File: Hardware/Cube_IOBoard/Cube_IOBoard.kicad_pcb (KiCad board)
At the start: 2 copper layers, 50.5 x 50.4 mm, 14 parts, among them J10 Pixhawk_Cube_DF17_Module_Bus_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, J11 GPS1 & I2C1, J12 GPS2 & I2C2, J13 TELEM2, J2 USB, LED & BUZZER, J4 ADC, J5 CAN2, J6 I2C2, J7 TELEM1, J8 CAN1

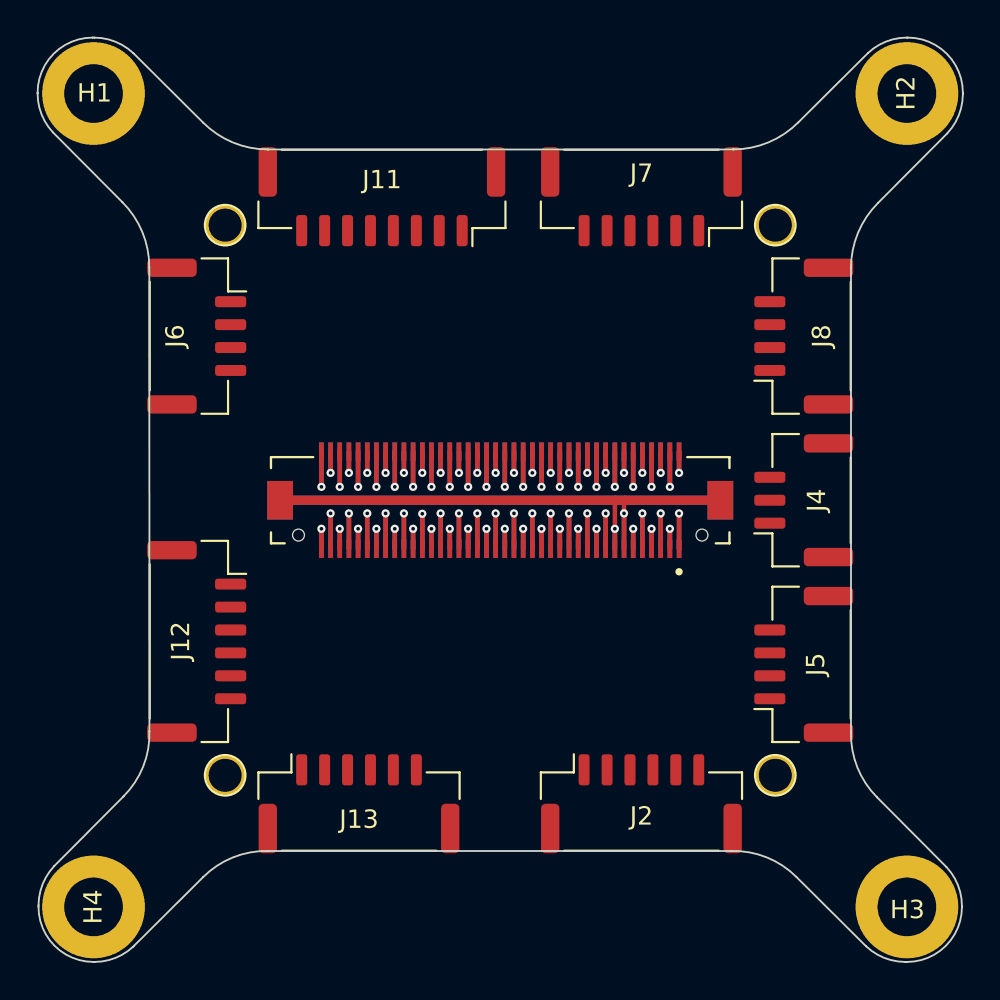
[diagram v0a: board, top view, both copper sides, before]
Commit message: Added labels to the connectors
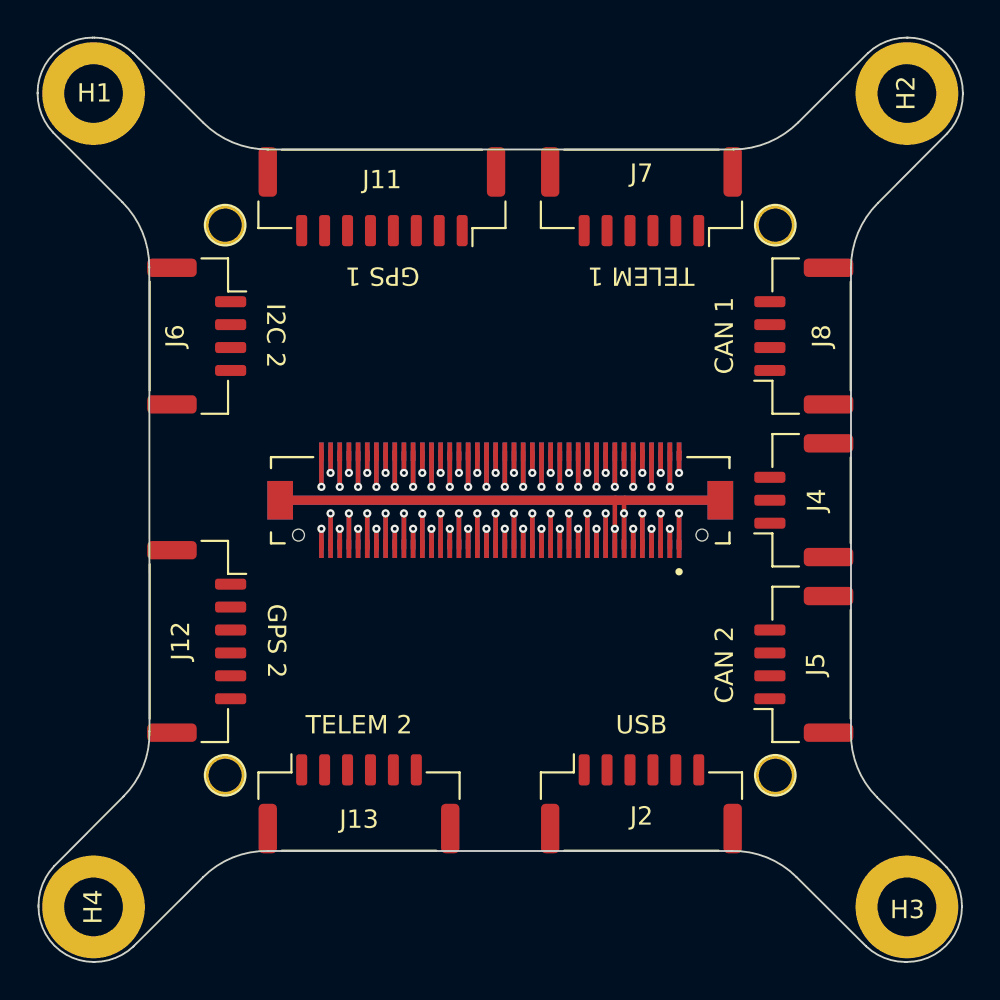
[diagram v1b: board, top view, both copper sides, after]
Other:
- board text added: "CAN 1"
- board text added: "CAN 2"
- board text added: "GPS 1"
- board text added: "GPS 2"
- board text added: "I2C 2"
- board text added: "TELEM 1"
- board text added: "TELEM 2"
- board text added: "USB"
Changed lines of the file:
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@@
   (gr_arc (start 128.41 88.575) (mid 130.325331 88.919911) (end 131.95 89.991316) (layer "Edge.Cuts") (width 0.1))
   (gr_line (start 93.575 44.224999) (end 93.675 44.225) (layer "Edge.Cuts") (width 0.1))
+  (gr_text "GPS 1" (at 109.375 57.225 180) (layer "F.SilkS")
+    (effects (font (size 1 1) (thickness 0.15)))
+  )
+  (gr_text "GPS 2" (at 103.6 77.125 270) (layer "F.SilkS")
+    (effects (font (size 1 1) (thickness 0.15)))
+  )
+  (gr_text "TELEM 1" (at 123.475 57.225 180) (layer "F.SilkS")
+    (effects (font (size 1 1) (thickness 0.15)))
+  )
+  (gr_text "I2C 2" (at 103.55 60.475 270) (layer "F.SilkS")
+    (effects (font (size 1 1) (thickness 0.15)))
+  )
+  (gr_text "USB" (at 123.5 81.7) (layer "F.SilkS")
+    (effects (font (size 1 1) (thickness 0.15)))
+  )
+  (gr_text "TELEM 2" (at 108.1 81.7) (layer "F.SilkS")
+    (effects (font (size 1 1) (thickness 0.15)))
+  )
+  (gr_text "CAN 1" (at 128.025 60.475 90) (layer "F.SilkS")
+    (effects (font (size 1 1) (thickness 0.15)))
+  )
+  (gr_text "CAN 2" (at 128.025 78.425 90) (layer "F.SilkS")
+    (effects (font (size 1 1) (thickness 0.15)))
+  )
   (segment (start 127.800001 69.45) (end 122.595502 69.45) (width 0.5) (layer "F.Cu") (net 1))
   (segment (start 122.550001 69.495501) (end 122.595502 69.45) (width 0.25) (layer "F.Cu") (net 1))

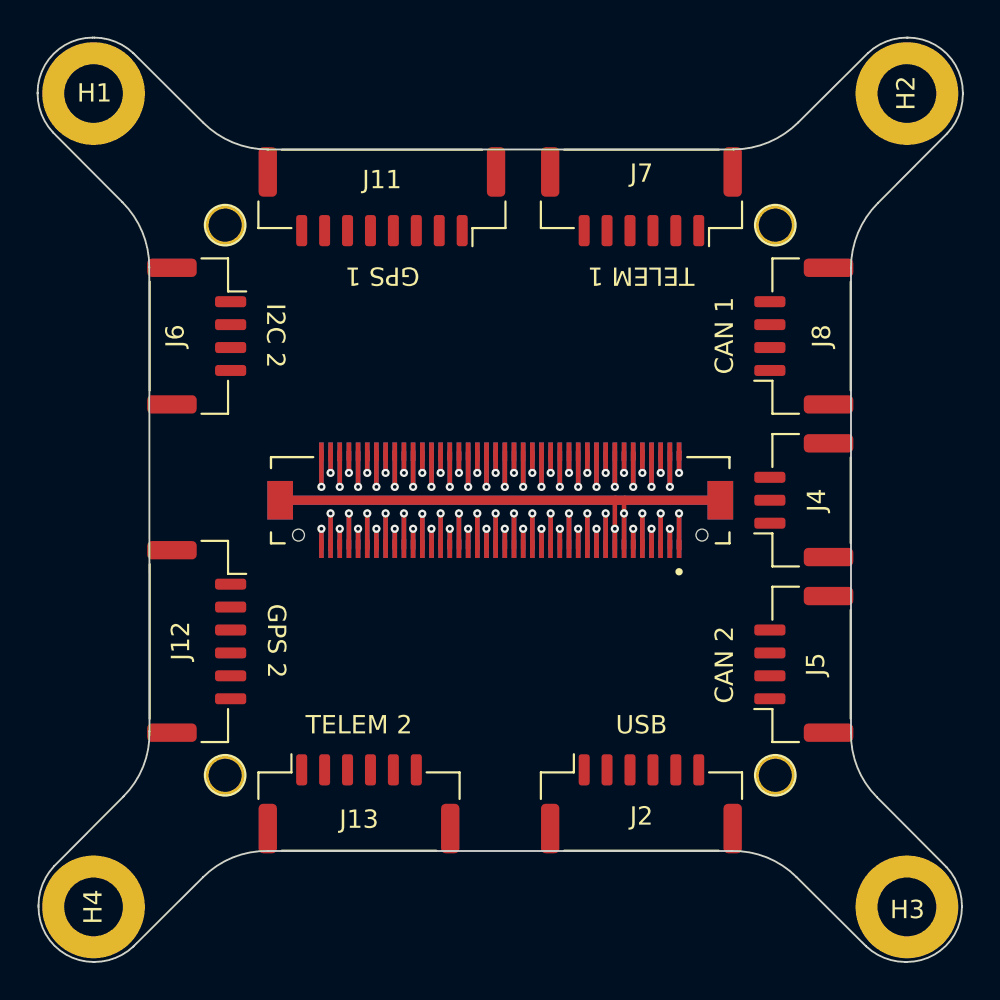
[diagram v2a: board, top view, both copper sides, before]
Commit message: Added EMI filters and TVS to IO schematic, experimenting with spice sims
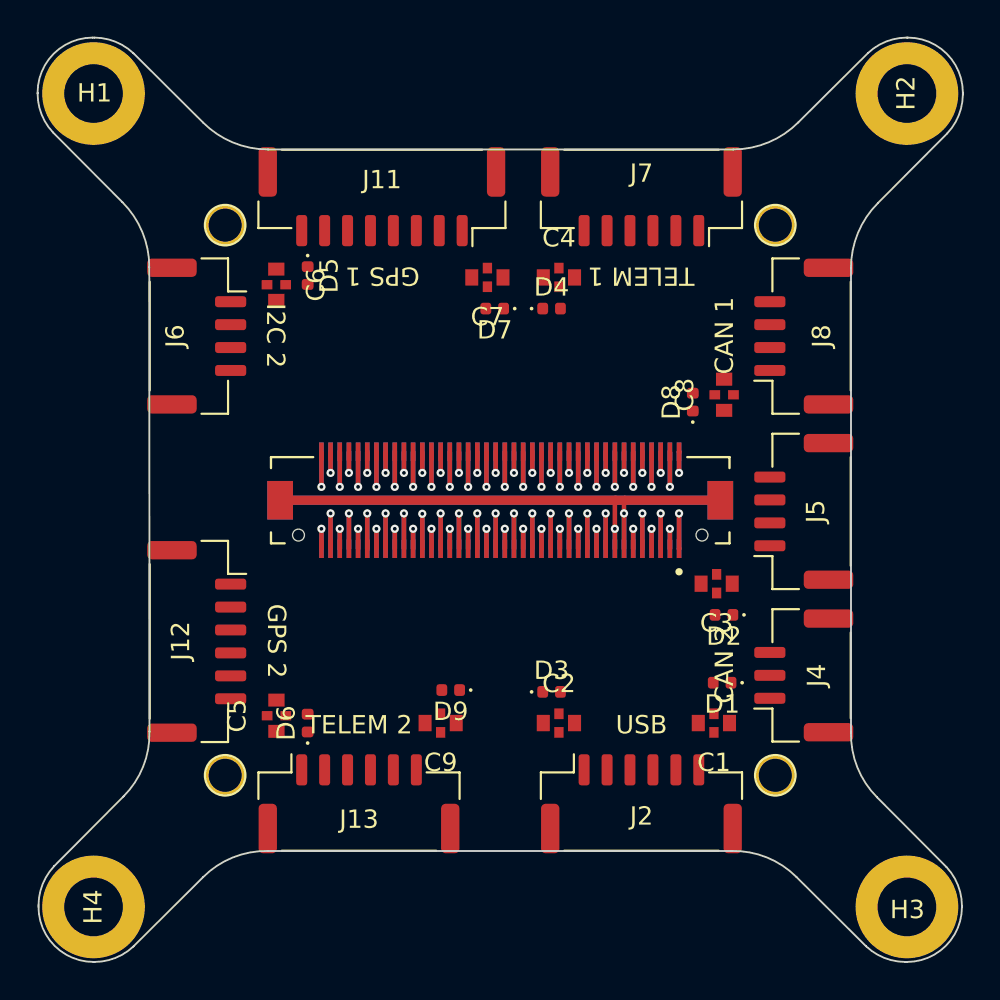
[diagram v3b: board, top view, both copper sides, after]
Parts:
- added C1: KNH16C104DA5TS, libraries:KNH16C104DA5TS, F.Cu at (127.5, 81.6)
- added C2: KNH16C104DA5TS, libraries:KNH16C104DA5TS, F.Cu at (119.0, 81.6)
- added C3: KNH16C104DA5TS, libraries:KNH16C104DA5TS, F.Cu at (127.6, 74.0)
- added C4: KNH16C104DA5TS, libraries:KNH16C104DA5TS, F.Cu at (119.0, 57.3)
- added C5: KNH16C104DA5TS, libraries:KNH16C104DA5TS, F.Cu at (103.6, 81.2)
- added C6: KNH16C104DA5TS, libraries:KNH16C104DA5TS, F.Cu at (103.6, 57.7)
- added C7: KNH16C104DA5TS, libraries:KNH16C104DA5TS, F.Cu at (115.1, 57.3)
- added C8: KNH16C104DA5TS, libraries:KNH16C104DA5TS, F.Cu at (128.0, 63.7)
- added C9: KNH16C104DA5TS, libraries:KNH16C104DA5TS, F.Cu at (112.6, 81.6)
- added D1: PESD0402-140, Diode_SMD:D_0402_1005Metric, F.Cu at (127.9, 79.4)
- added D2: PESD0402-140, Diode_SMD:D_0402_1005Metric, F.Cu at (128.0, 75.7)
- added D3: PESD0402-140, Diode_SMD:D_0402_1005Metric, F.Cu at (118.6, 79.9)
- added D4: PESD0402-140, Diode_SMD:D_0402_1005Metric, F.Cu at (118.6, 59.0)
- added D5: PESD0402-140, Diode_SMD:D_0402_1005Metric, F.Cu at (105.3, 57.2)
- added D6: PESD0402-140, Diode_SMD:D_0402_1005Metric, F.Cu at (105.3, 81.6)
- added D7: PESD0402-140, Diode_SMD:D_0402_1005Metric, F.Cu at (115.5, 59.0)
- added D8: PESD0402-140, Diode_SMD:D_0402_1005Metric, F.Cu at (126.3, 64.1)
- added D9: PESD0402-140, Diode_SMD:D_0402_1005Metric, F.Cu at (113.1, 79.8)
- moved J4 9.55 mm to (132.3, 79.0)
- moved J5 8.34 mm to (132.3, 70.1)
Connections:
- J10 pad 27: unconnected-(J10-Pad27) -> /~{VDD_5V_PERIPH_EN}
- J10 pad 29: unconnected-(J10-Pad29) -> /VBUS
- J10 pad 55: unconnected-(J10-Pad55) -> /~{VDD_BRICK_VALID}
- J10 pad 57: unconnected-(J10-Pad57) -> /~{VDD_BACKUP_VALID}
- J10 pad 59: unconnected-(J10-Pad59) -> /~{VBUS_VALID}
- J10 pad 61: unconnected-(J10-Pad61) -> /VDD_5V_IN_PROT
- J10 pad 63: unconnected-(J10-Pad63) -> /VDD_5V_IN_PROT
- J10 pad 9: unconnected-(J10-Pad9) -> /VDD_SERVO_IN
- J11 pad 1: unconnected-(J11-Pad1) -> Net-(J11-Pad1)
- J12 pad 1: unconnected-(J12-Pad1) -> Net-(J12-Pad1)
- J13 pad 1: unconnected-(J13-Pad1) -> Net-(J13-Pad1)
- J2 pad 1: /VBUS -> Net-(J2-Pad1)
- J4 pad 1: unconnected-(J4-Pad1) -> Net-(J4-Pad1)
- J5 pad 1: unconnected-(J5-Pad1) -> Net-(J5-Pad1)
- J6 pad 1: unconnected-(J6-Pad1) -> Net-(J6-Pad1)
- J7 pad 1: unconnected-(J7-Pad1) -> Net-(J7-Pad1)
- J8 pad 1: unconnected-(J8-Pad1) -> Net-(J8-Pad1)
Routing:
- net /VDD_5V_IN_PROT: track 0.00 -> 6.05 mm, vias 0 -> 2
- net unconnected-(J10-Pad9): track 3.87 -> 0.00 mm, vias 1 -> 0
- net unconnected-(J10-Pad61): track 3.87 -> 0.00 mm, vias 1 -> 0
- net unconnected-(J10-Pad29): track 3.87 -> 0.00 mm, vias 1 -> 0
- net /VDD_SERVO_IN: track 0.00 -> 3.87 mm, vias 0 -> 1
- net /VBUS: track 0.00 -> 3.87 mm, vias 0 -> 1
- net unconnected-(J10-Pad57): track 3.85 -> 0.00 mm, vias 1 -> 0
- net /~{VDD_BACKUP_VALID}: track 0.00 -> 3.85 mm, vias 0 -> 1
- net unconnected-(J10-Pad59): track 2.19 -> 0.00 mm, vias 1 -> 0
- net /~{VBUS_VALID}: track 0.00 -> 2.19 mm, vias 0 -> 1
- net unconnected-(J10-Pad63): track 2.19 -> 0.00 mm, vias 1 -> 0
- net unconnected-(J10-Pad55): track 2.19 -> 0.00 mm, vias 1 -> 0
- net unconnected-(J10-Pad27): track 2.19 -> 0.00 mm, vias 1 -> 0
- net /~{VDD_BRICK_VALID}: track 0.00 -> 2.19 mm, vias 0 -> 1
- net /~{VDD_5V_PERIPH_EN}: track 0.00 -> 2.19 mm, vias 0 -> 1
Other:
- copper layers 2 -> 4

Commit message: Arranged and routed IO connectors
It looks like the VDD 5V Periph is supposed to come from the PSM, either I add pins to connect to a separate module or the entire PSM needs to be implemented on this board...**gulp**
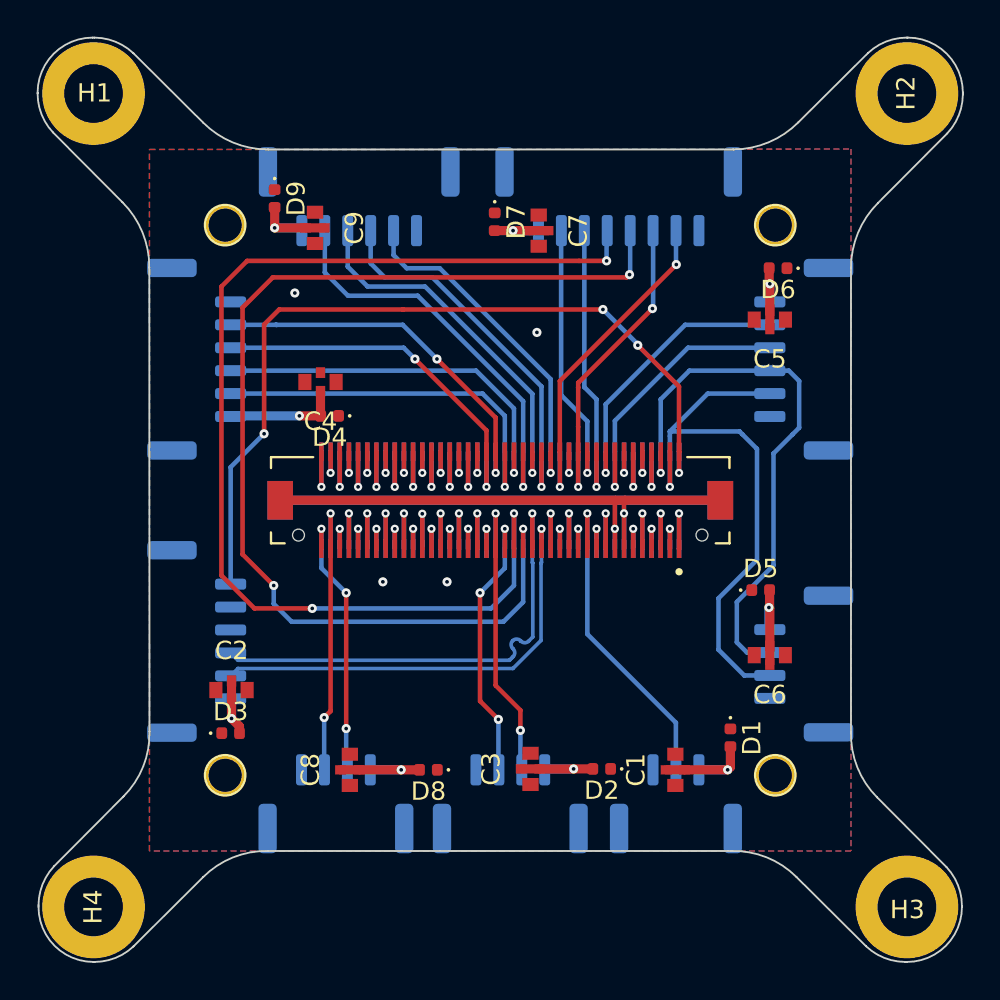
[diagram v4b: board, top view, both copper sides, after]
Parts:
- J11, J12, J13, J2, J4, J5, J6, J7, J8: moved to B.Cu
- moved J6 37.6 mm to (132.3, 78.4)
- moved J12 36.5 mm to (132.3, 61.8)
- moved J8 36.1 mm to (106.8, 86.0), turned to 180 degrees
- moved D6 35.7 mm to (130.9, 56.8), turned to 180 degrees
- moved C5 34.5 mm to (130.5, 59.6), turned to 0 degrees
- moved C6 33.6 mm to (130.5, 77.9), turned to 0 degrees
- moved J13 33.1 mm to (108.1, 52.9)
- moved D5 30.1 mm to (130.0, 74.3), turned to 0 degrees
- moved C8 28.9 mm to (107.6, 84.2)
- moved D9 28.5 mm to (103.5, 53.0), turned to -90 degrees
- moved C9 27.9 mm to (105.7, 54.6), turned to 90 degrees
- moved J7 25.8 mm to (99.2, 61.8), turned to 90 degrees
- moved J2 25.8 mm to (99.2, 77.2), turned to 90 degrees
- moved D8 24.7 mm to (111.9, 84.2), turned to 180 degrees
- moved J5 22.6 mm to (116.3, 86.0), turned to 180 degrees
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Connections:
- C1 pad 1: unconnected-(C1-Pad1) -> /VDD_5V_PERIPH
- J10 pad 31: unconnected-(J10-Pad31) -> /USB_OTG+
- J10 pad 33: unconnected-(J10-Pad33) -> /USB_OTG-
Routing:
- net /I2C1_SDA: track 2.19 -> 60.7 mm, vias 1 -> 3
- net /I2C1_SCL: track 3.87 -> 62.1 mm, vias 1 -> 3
- net /FMU_LED_AMBER: track 2.33 -> 45.5 mm, vias 1 -> 4
- net /I2C2_SCL: track 2.32 -> 31.3 mm
- net /I2C2_SDA: track 3.84 -> 31.6 mm
- net /USB_OTG-: track 0.00 -> 26.5 mm, vias 0 -> 1
- net /USB_OTG+: track 0.00 -> 24.9 mm, vias 0 -> 1
- net /SERIAL2_TX: track 3.84 -> 22.6 mm
- net /SERIAL1_RX: track 2.32 -> 21.0 mm
- net /SERIAL1_RTS: track 2.32 -> 20.7 mm, vias 1 -> 2
- net /SERIAL2_RX: track 2.32 -> 20.4 mm
- net /SERIAL2_CTS: track 3.84 -> 21.3 mm
- net /SERIAL1_TX: track 3.84 -> 21.2 mm
- net /SERIAL1_CTS: track 3.84 -> 20.8 mm, vias 1 -> 2
- net /SERIAL2_RTS: track 2.32 -> 19.0 mm
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- added copper zone on B.Cu, net GND
- added copper zone on F.Cu, net GND
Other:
- copper layers 4 -> 2
- board text added: "ADC"
